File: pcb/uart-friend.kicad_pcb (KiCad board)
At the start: 2 copper layers, 31.1 x 16.5 mm, 22 parts, among them P1 USB_OTG, P3 CONN_01X03, P4 CONN_01X03, P5 CONN_01X06, P6 CONN_01X03, Q1 Q_PMOS_GSD, U1 AP7365_ADJ_SOT-23-5, U2 CY7C65213-SSOP

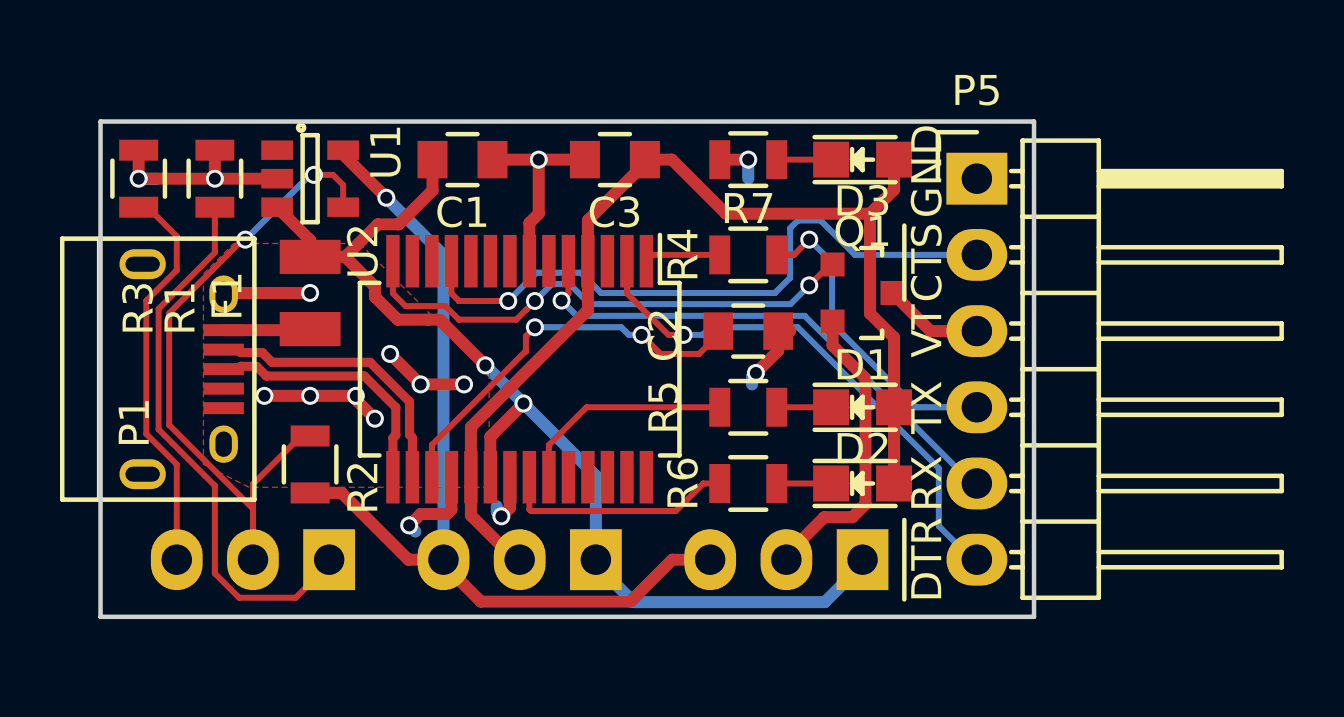
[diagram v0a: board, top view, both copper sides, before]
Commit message: update vias to 2:1 apr, make 2 up for production
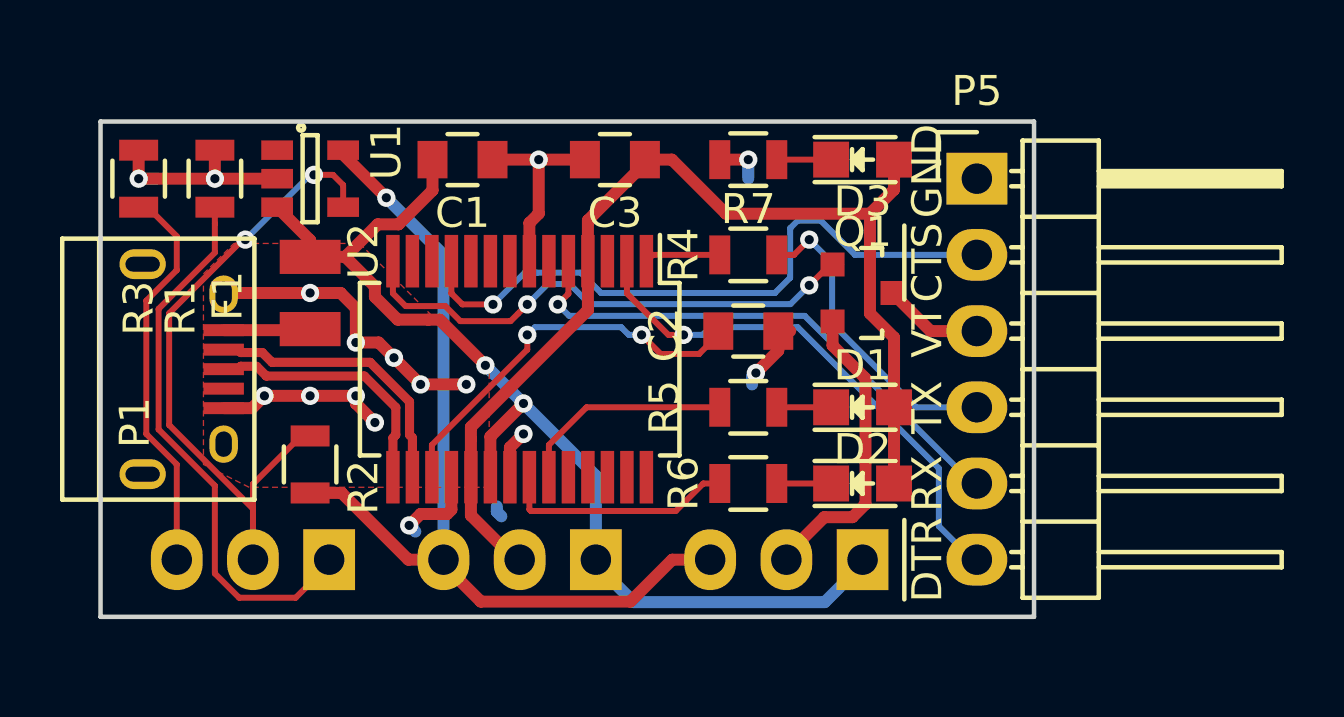
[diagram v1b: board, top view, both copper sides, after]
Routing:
- net GND: track 25.6 -> 38.3 mm, vias 8 -> 16
- net (no net): track 7.01 -> 0.40 mm, vias 7 -> 0
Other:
- net class Default: via_dia 0.6 -> 0.6096; via_drill 0.4 -> 0.3048
- net class Power: via_dia 0.6 -> 0.6096; via_drill 0.4 -> 0.3048
- net class USB Signal: via_dia 0.6 -> 0.6096; via_drill 0.4 -> 0.3048
- rule via_min_size: 0.4 -> 0.3
